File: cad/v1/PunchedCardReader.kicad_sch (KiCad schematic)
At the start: 53 parts

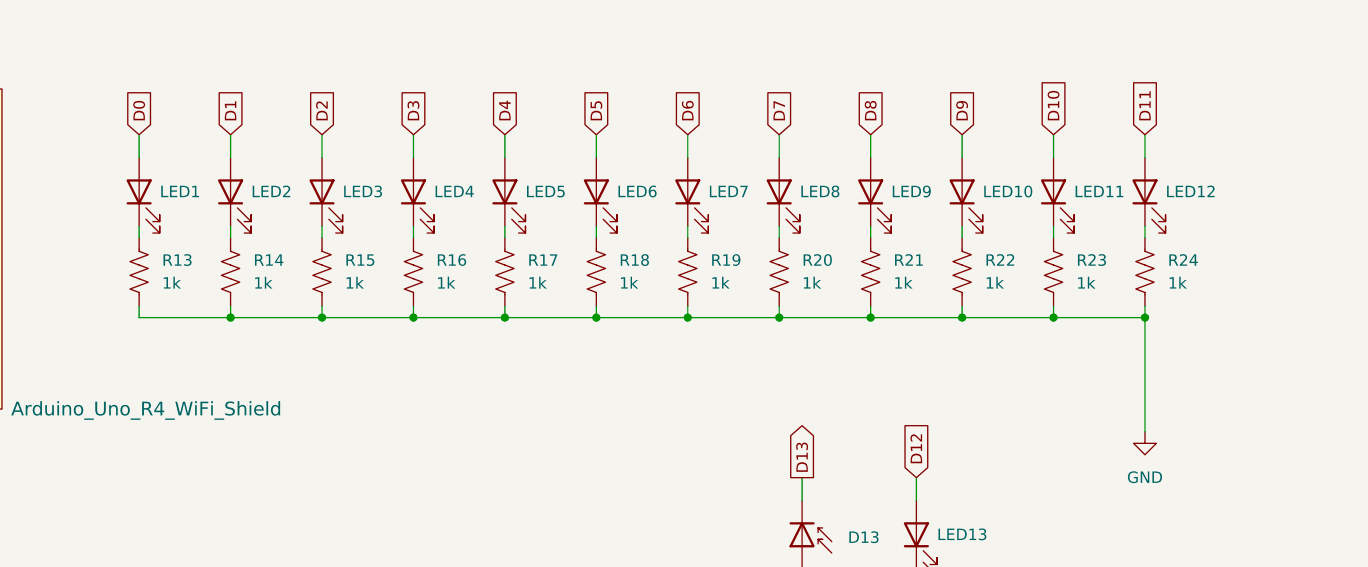
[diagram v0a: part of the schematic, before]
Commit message: Update photodiode resistor value and upload current hardware test code
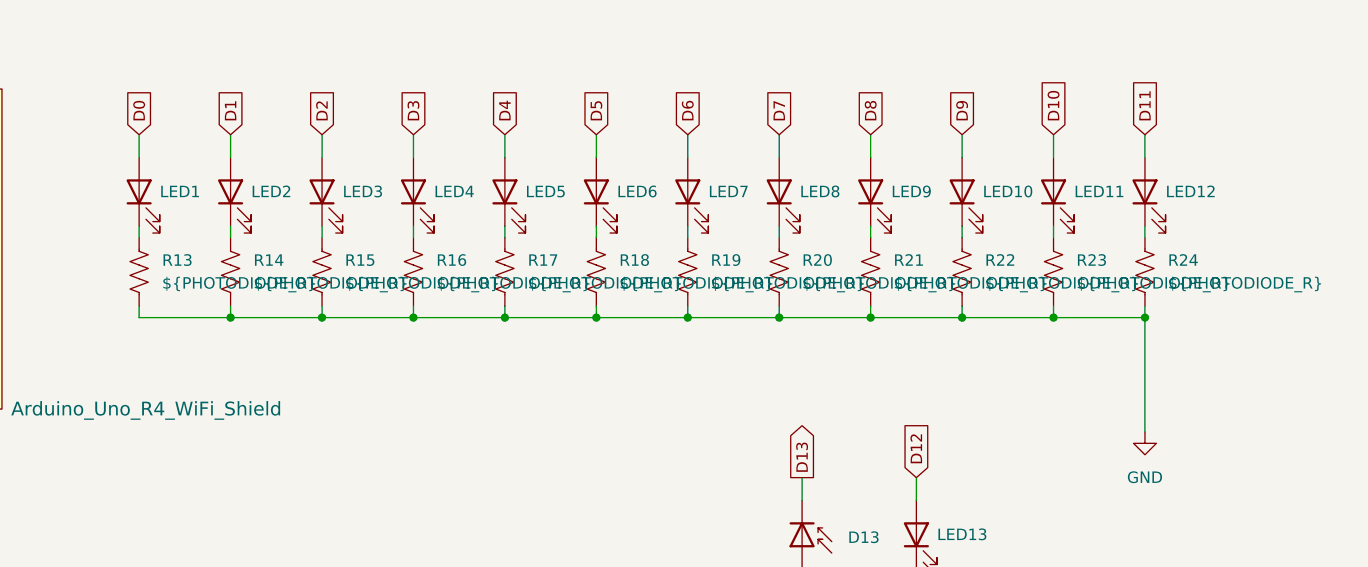
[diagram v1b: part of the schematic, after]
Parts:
- R13, R14, R15, R16, R17, R18, R19, R20, R21, R22, R23, R24: value 1k -> ${PHOTODIODE_R}
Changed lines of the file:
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@@
 			)
 		)
-		(property "Value" "1k"
+		(property "Value" "${PHOTODIODE_R}"
 			(at 231.14 59.6899 0)
 			(effects
@@
 			)
 		)
-		(property "Value" "1k"
+		(property "Value" "${PHOTODIODE_R}"
 			(at 210.82 59.6899 0)
 			(effects
@@
 			)
 		)
-		(property "Value" "1k"
+		(property "Value" "${PHOTODIODE_R}"
 			(at 170.18 59.6899 0)
 			(effects
@@
 			)
 		)
-		(property "Value" "1k"
+		(property "Value" "${PHOTODIODE_R}"
 			(at 190.5 59.6899 0)
 			(effects
@@
 			)
 		)
-		(property "Value" "1k"
+		(property "Value" "${PHOTODIODE_R}"
 			(at 220.98 59.6899 0)
 			(effects
@@
 			)
 		)
-		(property "Value" "1k"
+		(property "Value" "${PHOTODIODE_R}"
 			(at 149.86 59.6899 0)
 			(effects
@@
 			)
 		)
-		(property "Value" "1k"
+		(property "Value" "${PHOTODIODE_R}"
 			(at 139.7 59.6899 0)
 			(effects
@@
 			)
 		)
-		(property "Value" "1k"
+		(property "Value" "${PHOTODIODE_R}"
 			(at 160.02 59.6899 0)
 			(effects
@@
 			)
 		)
-		(property "Value" "1k"
+		(property "Value" "${PHOTODIODE_R}"
 			(at 180.34 59.6899 0)
 			(effects
@@
 			)
 		)
-		(property "Value" "1k"
+		(property "Value" "${PHOTODIODE_R}"
 			(at 251.46 59.6899 0)
 			(effects
@@
 			)
 		)
-		(property "Value" "1k"
+		(property "Value" "${PHOTODIODE_R}"
 			(at 241.3 59.6899 0)
 			(effects
@@
 			)
 		)
-		(property "Value" "1k"
+		(property "Value" "${PHOTODIODE_R}"
 			(at 200.66 59.6899 0)
 			(effects

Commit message: Implement pre-read on/off calibration read
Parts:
- renumbered D9 to D1, D6 to D10, D10 to D2, D7 to D3, D8 to D4, D1 to D5, D2 to D6, D3 to D7, D4 to D8, D5 to D9, R9 to R1, R6 to R10, R10 to R2, R7 to R3, R8 to R4, R1 to R5, R2 to R6, R3 to R7, R4 to R8, R5 to R9
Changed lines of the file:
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@@
 	(title_block
 		(title "Punched Card Reader")
-		(date "2025-11-17")
-		(rev "1.0")
+		(date "2025-12-01")
+		(rev "1.2")
 		(company "Brown University")
 		(comment 1 "Configure pin D13 on the UNO R4 to be analog input with the Renesas API")
@@
 		(dnp no)
 		(fields_autoplaced yes)
-		(property "Reference" "D6"
+		(property "Reference" "D10"
 			(at 215.9 123.5074 90)
 			(effects
@@
 			(project "PunchedCardReader"
 				(path "/111b8190-4ed9-4f5f-a67b-08bb7c2eb253"
-					(reference "D6")
+					(reference "D10")
 					(unit 1)
 				)
@@
 		(dnp no)
 		(fields_autoplaced yes)
-		(property "Reference" "D5"
+		(property "Reference" "D9"
 			(at 203.2 123.5074 90)
 			(effects
@@
 			(project "PunchedCardReader"
 				(path "/111b8190-4ed9-4f5f-a67b-08bb7c2eb253"
-					(reference "D5")
+					(reference "D9")
 					(unit 1)
 				)
@@
 		(dnp no)
 		(fields_autoplaced yes)
-		(property "Reference" "R3"
+		(property "Reference" "R7"
 			(at 162.56 132.0799 0)
 			(effects
@@
 			(project "PunchedCardReader"
 				(path "/111b8190-4ed9-4f5f-a67b-08bb7c2eb253"
-					(reference "R3")
+					(reference "R7")
 					(unit 1)
 				)
@@
 		(dnp no)
 		(fields_autoplaced yes)
-		(property "Reference" "D4"
+		(property "Reference" "D8"
 			(at 177.8 123.5074 90)
 			(effects
@@
 			(project "PunchedCardReader"
 				(path "/111b8190-4ed9-4f5f-a67b-08bb7c2eb253"
-					(reference "D4")
+					(reference "D8")
 					(unit 1)
 				)
@@
 		(dnp no)
 		(fields_autoplaced yes)
-		(property "Reference" "D8"
+		(property "Reference" "D4"
 			(at 101.6 123.5074 90)
 			(effects
@@
 			(project "PunchedCardReader"
 				(path "/111b8190-4ed9-4f5f-a67b-08bb7c2eb253"
-					(reference "D8")
+					(reference "D4")
 					(unit 1)
 				)
@@
 		(dnp no)
 		(fields_autoplaced yes)
-		(property "Reference" "R1"
+		(property "Reference" "R5"
 			(at 124.46 132.0799 0)
 			(effects
@@
 			(project ""
 				(path "/111b8190-4ed9-4f5f-a67b-08bb7c2eb253"
-					(reference "R1")
+					(reference "R5")
 					(unit 1)
 				)
@@
 		(dnp no)
 		(fields_autoplaced yes)
-		(property "Reference" "D10"
+		(property "Reference" "D2"
 			(at 63.5 123.5074 90)
 			(effects
@@
 			(project "PunchedCardReader"
 				(path "/111b8190-4ed9-4f5f-a67b-08bb7c2eb253"
-					(reference "D10")
+					(reference "D2")
 					(unit 1)
 				)
@@
 		(dnp no)
 		(fields_autoplaced yes)
-		(property "Reference" "R5"
+		(property "Reference" "R9"
 			(at 200.66 132.0799 0)
 			(effects
@@
 			(project "PunchedCardReader"
 				(path "/111b8190-4ed9-4f5f-a67b-08bb7c2eb253"
-					(reference "R5")
+					(reference "R9")
 					(unit 1)
 				)
@@
 		(dnp no)
 		(fields_autoplaced yes)
-		(property "Reference" "D2"
+		(property "Reference" "D6"
 			(at 139.7 123.5074 90)
 			(effects
@@
 			(project "PunchedCardReader"
 				(path "/111b8190-4ed9-4f5f-a67b-08bb7c2eb253"
-					(reference "D2")
+					(reference "D6")
 					(unit 1)
 				)
@@
 		(dnp no)
 		(fields_autoplaced yes)
-		(property "Reference" "R10"
+		(property "Reference" "R2"
 			(at 60.96 132.0799 0)
 			(effects
@@
 			(project "PunchedCardReader"
 				(path "/111b8190-4ed9-4f5f-a67b-08bb7c2eb253"
-					(reference "R10")
+					(reference "R2")
 					(unit 1)
 				)
@@
 		(dnp no)
 		(fields_autoplaced yes)
-		(property "Reference" "D7"
+		(property "Reference" "D3"
 			(at 88.9 123.5074 90)
 			(effects
@@
 			(project "PunchedCardReader"
 				(path "/111b8190-4ed9-4f5f-a67b-08bb7c2eb253"
-					(reference "D7")
+					(reference "D3")
 					(unit 1)
 				)
@@
 		(dnp no)
 		(fields_autoplaced yes)
-		(property "Reference" "R7"
+		(property "Reference" "R3"
 			(at 86.36 132.0799 0)
 			(effects
@@
 			(project "PunchedCardReader"
 				(path "/111b8190-4ed9-4f5f-a67b-08bb7c2eb253"
-					(reference "R7")
+					(reference "R3")
 					(unit 1)
 				)
@@
 		(dnp no)
 		(fields_autoplaced yes)
-		(property "Reference" "D9"
+		(property "Reference" "D1"
 			(at 50.8 123.5074 90)
 			(effects
@@
 			(project "PunchedCardReader"
 				(path "/111b8190-4ed9-4f5f-a67b-08bb7c2eb253"
-					(reference "D9")
+					(reference "D1")
 					(unit 1)
 				)
@@
 		(dnp no)
 		(fields_autoplaced yes)
-		(property "Reference" "D1"
+		(property "Reference" "D5"
 			(at 127 123.5074 90)
 			(effects
@@
 			(project ""
 				(path "/111b8190-4ed9-4f5f-a67b-08bb7c2eb253"
-					(reference "D1")
+					(reference "D5")
 					(unit 1)
 				)
@@
 		(dnp no)
 		(fields_autoplaced yes)
-		(property "Reference" "R9"
+		(property "Reference" "R1"
 			(at 48.26 132.0799 0)
 			(effects
@@
 			(project "PunchedCardReader"
 				(path "/111b8190-4ed9-4f5f-a67b-08bb7c2eb253"
-					(reference "R9")
+					(reference "R1")
 					(unit 1)
 				)
@@
 		(dnp no)
 		(fields_autoplaced yes)
-		(property "Reference" "R6"
+		(property "Reference" "R10"
 			(at 213.36 132.0799 0)
 			(effects
@@
 			(project "PunchedCardReader"
 				(path "/111b8190-4ed9-4f5f-a67b-08bb7c2eb253"
-					(reference "R6")
+					(reference "R10")
 					(unit 1)
 				)
@@
 		(dnp no)
 		(fields_autoplaced yes)
-		(property "Reference" "R4"
+		(property "Reference" "R8"
 			(at 175.26 132.0799 0)
 			(effects
@@
 			(project "PunchedCardReader"
 				(path "/111b8190-4ed9-4f5f-a67b-08bb7c2eb253"
-					(reference "R4")
+					(reference "R8")
 					(unit 1)
 				)
@@
 		(dnp no)
 		(fields_autoplaced yes)
-		(property "Reference" "R8"
+		(property "Reference" "R4"
 			(at 99.06 132.0799 0)
 			(effects
@@
 			(project "PunchedCardReader"
 				(path "/111b8190-4ed9-4f5f-a67b-08bb7c2eb253"
-					(reference "R8")
+					(reference "R4")
 					(unit 1)
 				)
@@
 		(dnp no)
 		(fields_autoplaced yes)
-		(property "Reference" "D3"
+		(property "Reference" "D7"
 			(at 165.1 123.5074 90)
 			(effects
@@
 			(project "PunchedCardReader"
 				(path "/111b8190-4ed9-4f5f-a67b-08bb7c2eb253"
-					(reference "D3")
+					(reference "D7")
 					(unit 1)
 				)
@@
 		(dnp no)
 		(fields_autoplaced yes)
-		(property "Reference" "R2"
+		(property "Reference" "R6"
 			(at 137.16 132.0799 0)
 			(effects
@@
 			(project "PunchedCardReader"
 				(path "/111b8190-4ed9-4f5f-a67b-08bb7c2eb253"
-					(reference "R2")
+					(reference "R6")
 					(unit 1)
 				)

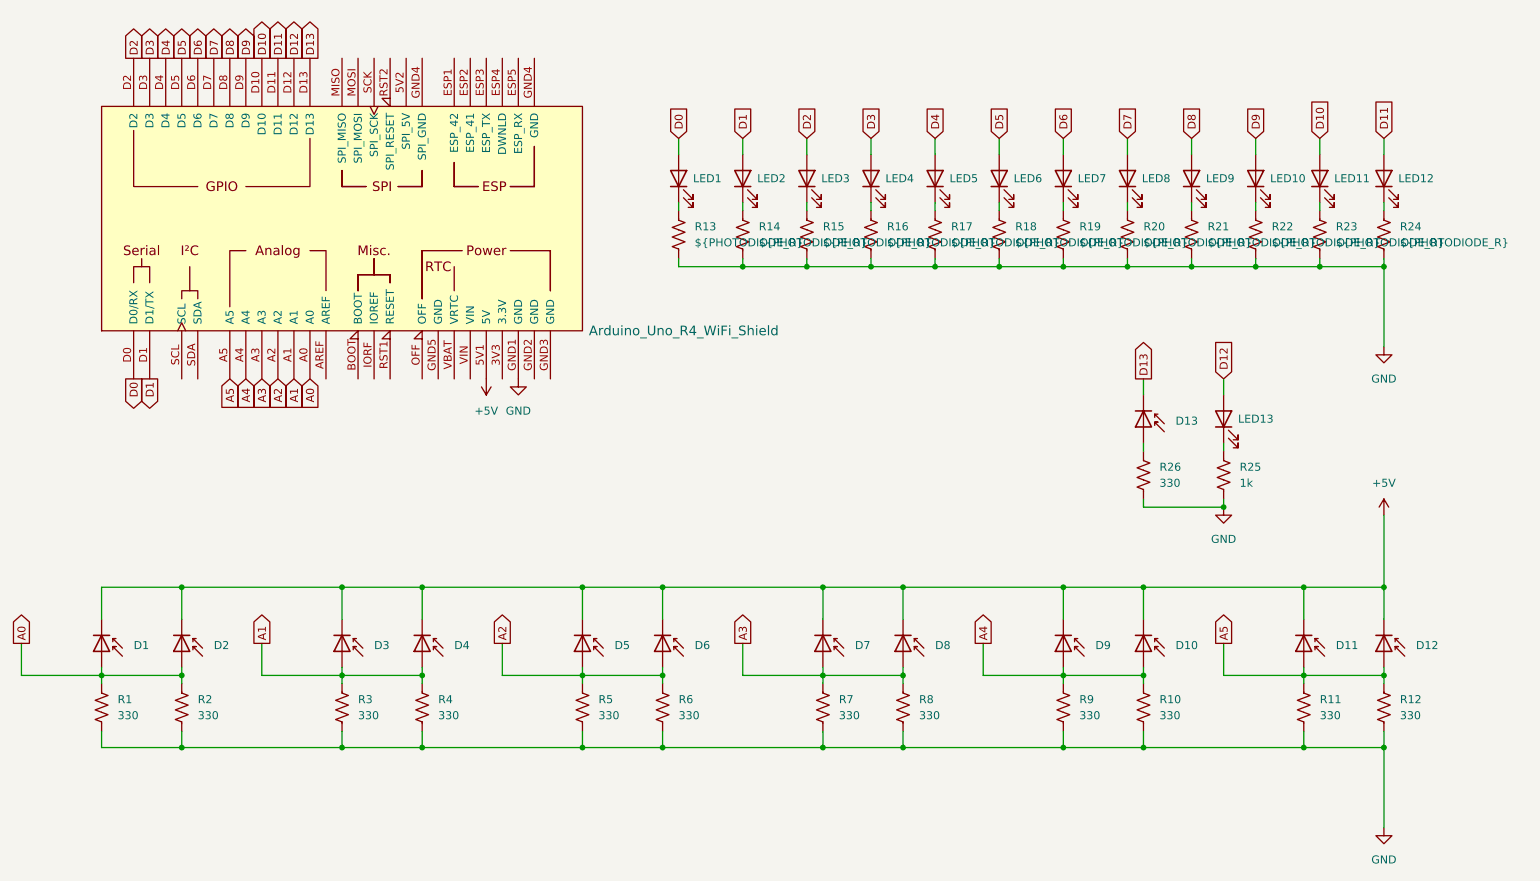
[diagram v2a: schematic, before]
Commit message: Fix stupid schematic blunder
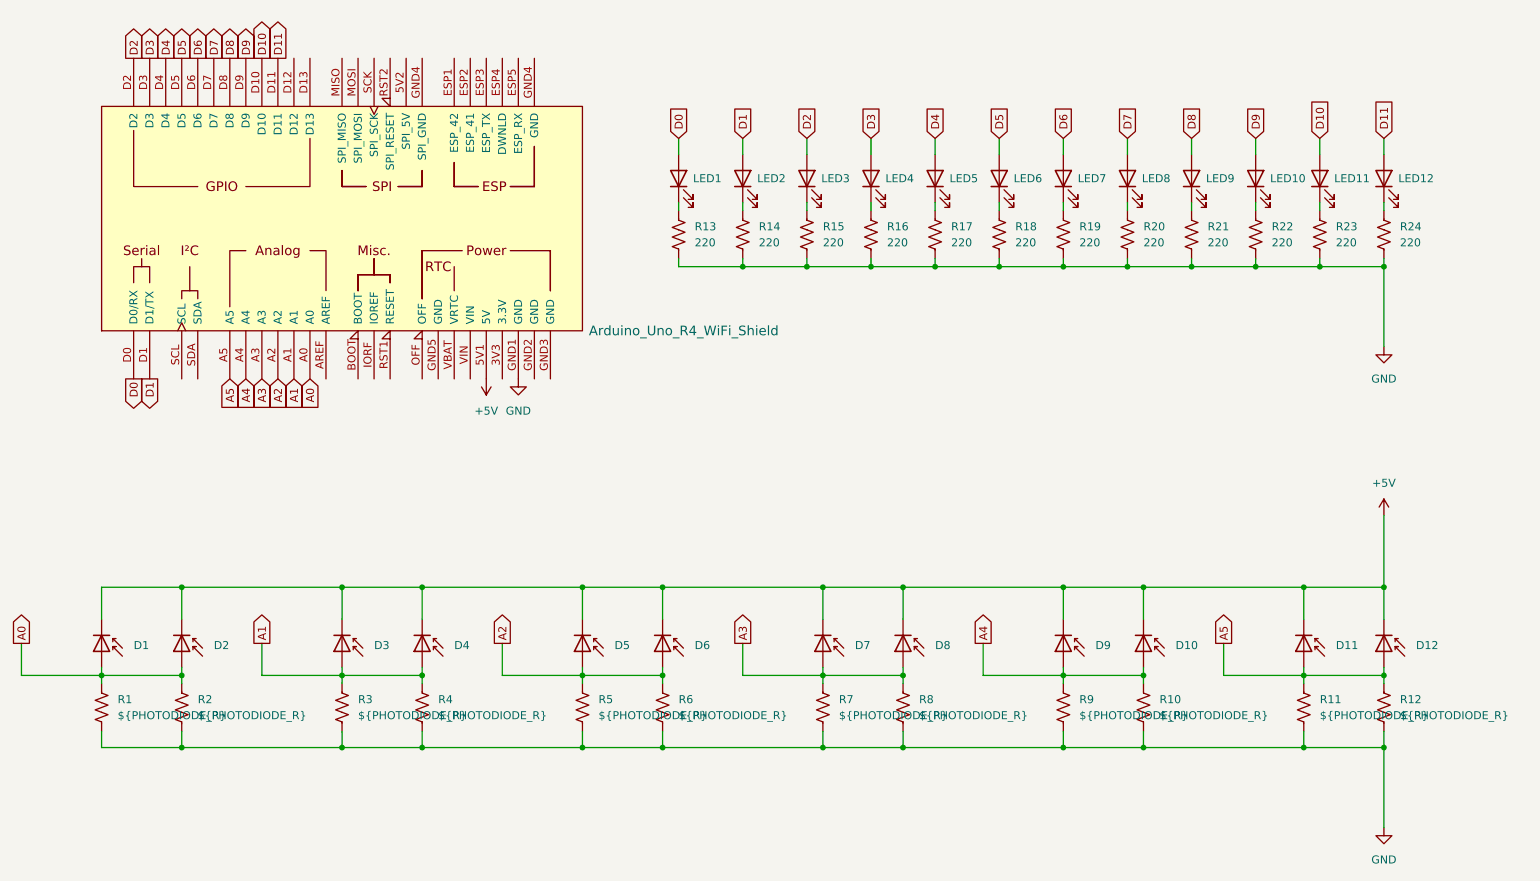
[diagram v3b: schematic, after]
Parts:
- removed D13: D_Photo, symbol Device:D_Photo
- removed LED13: LED, symbol Device:LED
- removed R25: 1k, symbol Device:R_US
- removed R26: 330, symbol Device:R_US
- R1, R10, R11, R12, R2, R3, R4, R5, R6, R7, R8, R9: value 330 -> ${PHOTODIODE_R}
- R13, R14, R15, R16, R17, R18, R19, R20, R21, R22, R23, R24: value ${PHOTODIODE_R} -> 220
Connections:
- net D12: no longer names the net of A1.D12
- net D13: no longer names the net of A1.D13
